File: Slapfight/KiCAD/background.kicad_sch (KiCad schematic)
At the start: 28 parts, among them U1K_ 74LS10, U1L_ 74LS86, U1M_ 74LS32, U1N_ 74LS00, U3L 74LS194, U3M 74LS194, U3N 74LS157, U3P 74LS157, U3Q 74LS157, U4K 74LS245, U4M 74LS245, U4N RAM_2016, U4P RAM_2016, U4Q 74LS157, U5Q 74LS174, U6H_SF_ 74LS32, U6K 27C256 - A77-08, U6M 27C256 - A77-08, U6N 27C256 - A77-07, U6P 27C256 - A77-05, U7J 74LS194, U7K 74LS194, U7L 74LS194, U7M 74LS194, U7N 74LS194, U7P 74LS194, U7Q 74LS157

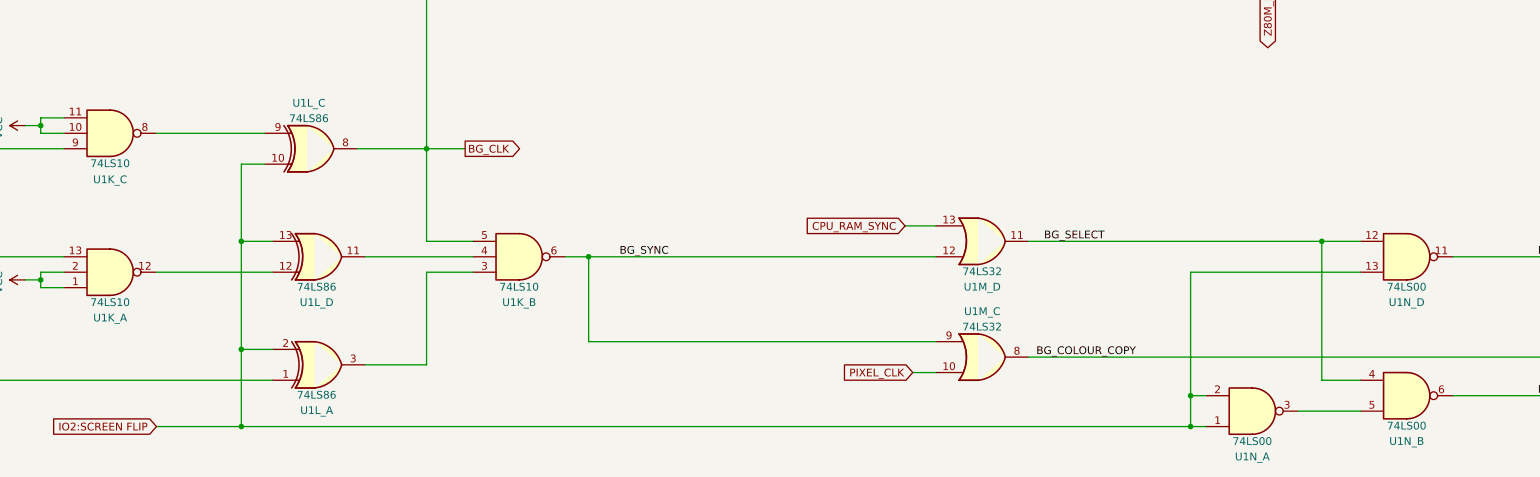
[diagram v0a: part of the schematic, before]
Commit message: Component naming updates
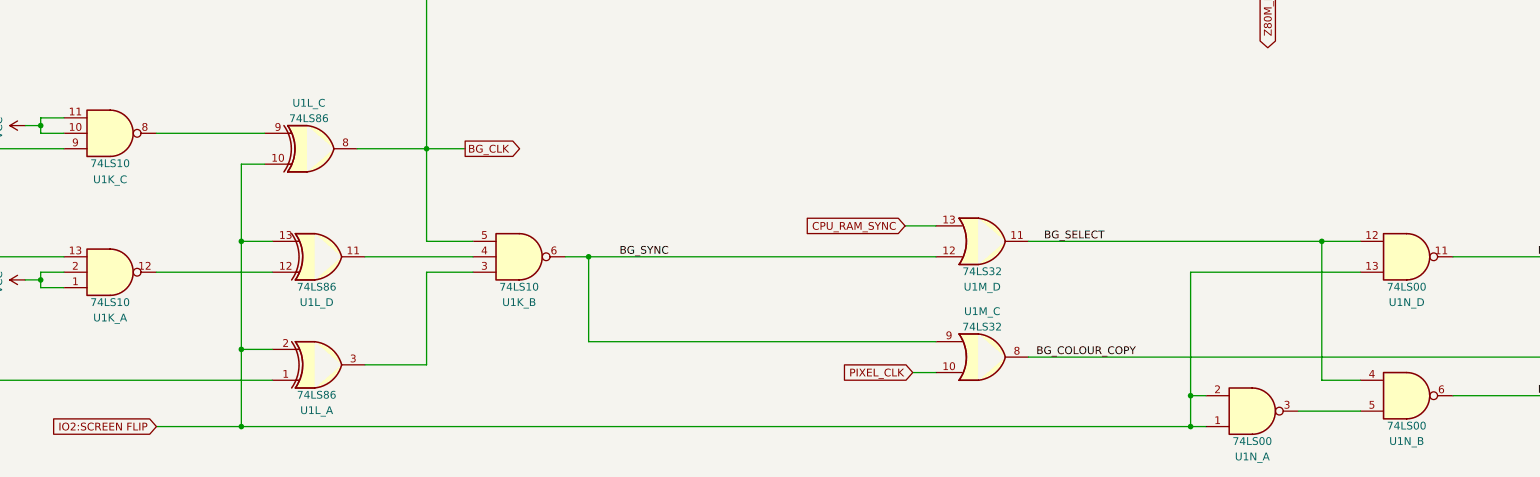
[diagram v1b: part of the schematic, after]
